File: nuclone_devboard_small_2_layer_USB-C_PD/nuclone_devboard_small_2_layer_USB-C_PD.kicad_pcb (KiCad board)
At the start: 2 copper layers, 50 x 50 mm, 39 parts, among them J1 JTAG_2X05, J2 TYPE-C-31-M-12, J3 nuclone_small_left, J4 nuclone_small_right, J5 Conn_02x06_Odd_Even, SW1 RESET, SW2 Bootloader, U1 MCP1702-MB

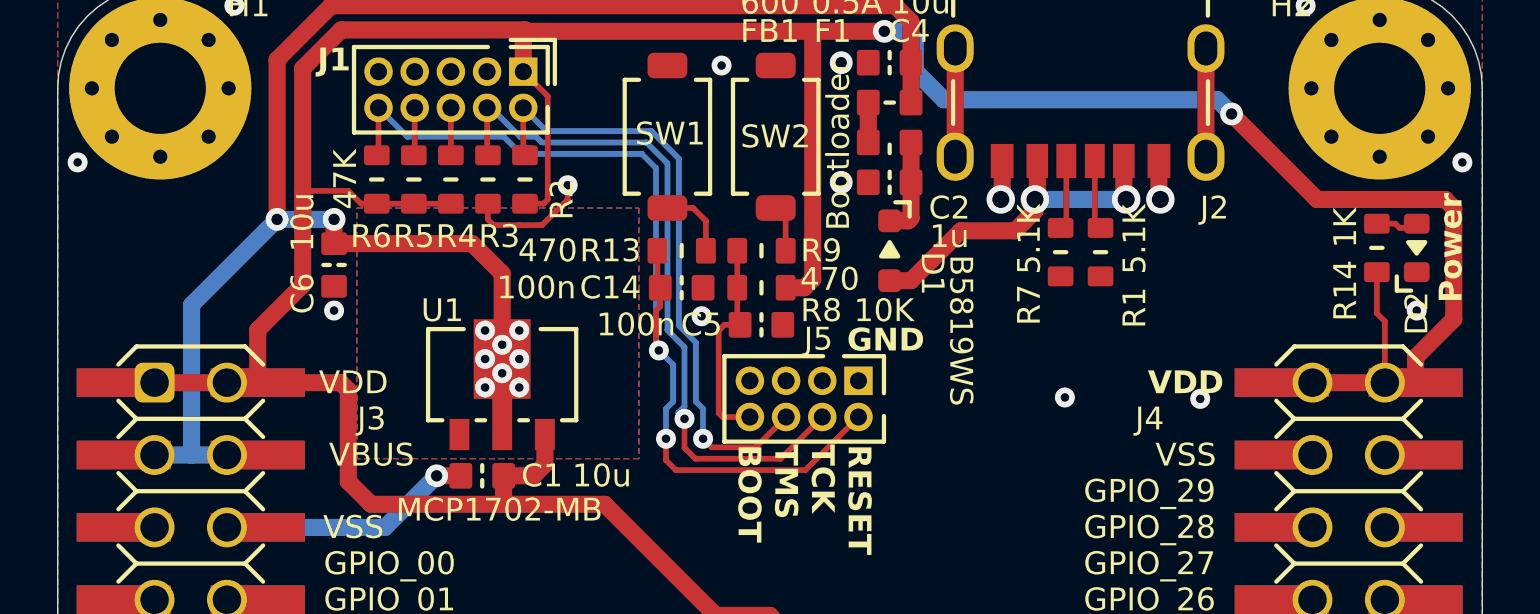
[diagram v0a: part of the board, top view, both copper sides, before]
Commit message: updated silkscreen
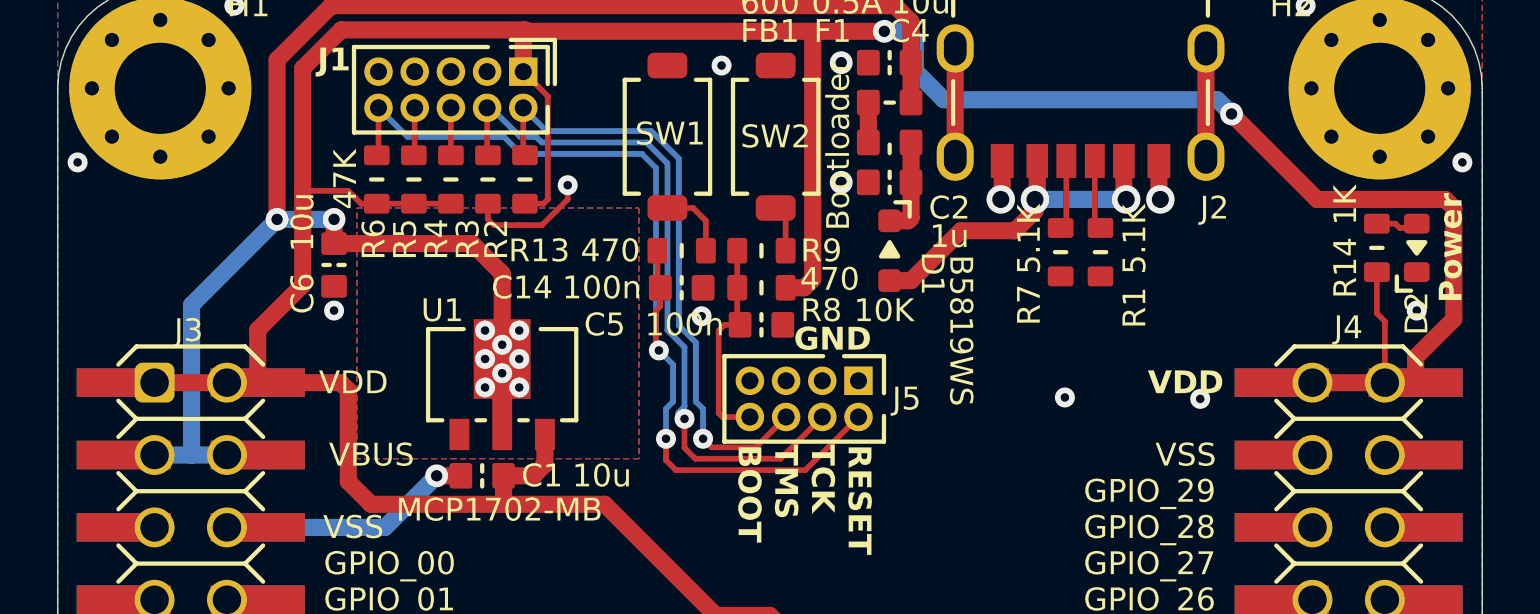
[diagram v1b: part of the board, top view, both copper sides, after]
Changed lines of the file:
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@@
     (property "ki_keywords" "Small nuclone right")
     (attr through_hole)
-    (fp_text reference "J4" (at 10.16 -6.985) (layer "F.SilkS")
+    (fp_text reference "J4" (at 13.36 -0.01) (layer "F.SilkS")
         (effects (font (size 0.8 0.8) (thickness 0.15)))
     )
@@
     (property "ki_keywords" "small nuclone")
     (attr through_hole)
-    (fp_text reference "J3" (at -10.16 -6.35) (layer "F.SilkS")
+    (fp_text reference "J3" (at -13.26 0.07) (layer "F.SilkS")
         (effects (font (size 0.8 0.8) (thickness 0.15)))
     )
@@
     (property "ki_keywords" "R res resistor")
     (attr smd)
-    (fp_text reference "R14" (at 1.5 1.1 -90) (layer "F.SilkS")
-        (effects (font (size 0.8 0.8) (thickness 0.15)))
-    )
-    (fp_text value "1K" (at -0.7 1.1 -90) (layer "F.SilkS")
+    (fp_text reference "R14" (at 0.7 1.1 -90) (layer "F.SilkS")
+        (effects (font (size 0.8 0.8) (thickness 0.15)))
+    )
+    (fp_text value "1K" (at -1.5 1.1 -90) (layer "F.SilkS")
         (effects (font (size 0.8 0.8) (thickness 0.15)))
     )
@@
     (property "ki_keywords" "R res resistor")
     (attr smd)
-    (fp_text reference "R3" (at 2 -0.4) (layer "F.SilkS")
+    (fp_text reference "R3" (at 2.1 0.7 90) (layer "F.SilkS")
         (effects (font (size 0.8 0.8) (thickness 0.15)))
     )
@@
     (property "ki_keywords" "R res resistor")
     (attr smd)
-    (fp_text reference "R13" (at -2.5 0) (layer "F.SilkS")
-        (effects (font (size 0.8 0.8) (thickness 0.15)))
-    )
-    (fp_text value "470" (at -4.7 0) (layer "F.SilkS")
+    (fp_text reference "R13" (at -5 0) (layer "F.SilkS")
+        (effects (font (size 0.8 0.8) (thickness 0.15)))
+    )
+    (fp_text value "470" (at -2.5 0) (layer "F.SilkS")
         (effects (font (size 0.8 0.8) (thickness 0.15)))
     )
@@
     (property "ki_keywords" "R res resistor")
     (attr smd)
-    (fp_text reference "R2" (at 0.7 -1.3 90) (layer "F.SilkS")
+    (fp_text reference "R2" (at 2.1 1 90) (layer "F.SilkS")
         (effects (font (size 0.8 0.8) (thickness 0.15)))
     )
@@
     (property "ki_keywords" "R res resistor")
     (attr smd)
-    (fp_text reference "R4" (at 2 -0.2) (layer "F.SilkS")
+    (fp_text reference "R4" (at 2.1 0.5 90) (layer "F.SilkS")
         (effects (font (size 0.8 0.8) (thickness 0.15)))
     )
@@
     (property "ki_keywords" "R res resistor")
     (attr smd)
-    (fp_text reference "R5" (at 2 0) (layer "F.SilkS")
+    (fp_text reference "R5" (at 2.1 0.3 90) (layer "F.SilkS")
         (effects (font (size 0.8 0.8) (thickness 0.15)))
     )
@@
     (property "ki_keywords" "R res resistor")
     (attr smd)
-    (fp_text reference "R6" (at 2 0.2) (layer "F.SilkS")
+    (fp_text reference "R6" (at 2.1 0.1 90) (layer "F.SilkS")
         (effects (font (size 0.8 0.8) (thickness 0.15)))
     )
@@
     (property "ki_keywords" "cap capacitor")
     (attr smd)
-    (fp_text reference "C14" (at 2.5 0) (layer "F.SilkS")
-        (effects (font (size 0.8 0.8) (thickness 0.15)))
-    )
-    (fp_text value "100n" (at 5.1 0) (layer "F.SilkS")
+    (fp_text reference "C14" (at 5.6 0) (layer "F.SilkS")
+        (effects (font (size 0.8 0.8) (thickness 0.15)))
+    )
+    (fp_text value "100n" (at 2.8 0) (layer "F.SilkS")
         (effects (font (size 0.8 0.8) (thickness 0.15)))
     )
@@
     (property "ki_keywords" "cap capacitor")
     (attr smd)
-    (fp_text reference "C5" (at -2.1 0) (layer "F.SilkS")
-        (effects (font (size 0.8 0.8) (thickness 0.15)))
-    )
-    (fp_text value "100n" (at -4.4 0) (layer "F.SilkS")
+    (fp_text reference "C5" (at -5.5 0) (layer "F.SilkS")
+        (effects (font (size 0.8 0.8) (thickness 0.15)))
+    )
+    (fp_text value "100n" (at -2.7 0) (layer "F.SilkS")
         (effects (font (size 0.8 0.8) (thickness 0.15)))
     )
@@
     (property "ki_keywords" "connector")
     (attr through_hole)
-    (fp_text reference "J5" (at -0.5 2.1 180) (layer "F.SilkS")
+    (fp_text reference "J5" (at -3.6 0 180) (layer "F.SilkS")
         (effects (font (size 0.8 0.8) (thickness 0.15)))
     )
@@
     (effects (font (size 0.8 0.8) (thickness 0.15) bold) (justify left bottom))
   )
-  (gr_text "GND" (at 57.7 42.9) (layer "F.SilkS")
-    (effects (font (size 0.8 0.8) (thickness 0.15) bold) (justify left bottom))
+  (gr_text "GND" (at 57.2 42.4) (layer "F.SilkS")
+    (effects (font (size 0.8 0.8) (thickness 0.15) bold))
   )
   (dimension (type aligned) (layer "Cmts.User")
